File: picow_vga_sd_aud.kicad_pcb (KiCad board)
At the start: 2 copper layers, 74.4 x 53.1 mm, 98 parts, among them J1 10103594-0001LF, J10 Micro_SD_Card, J2 AudioJack3, J3 Micro_SD_Card, J4 L77HDE15SD1CH4F, J5 TSW-102-07-G-S, J6 Conn_01x18_Pin, J7 Conn_02x03_Odd_Even, SW1 SW_Push, SW2 SW_Push, SW3 SW_Push, SW4 SW_Push, SW5 SW_boot, U1 TLV70033_SOT23-5, U10 ER_OLEDM0.91_1x-I2C, U2 PicoW, U3 NC7WZ16P6X, U4 NCP1117ST33T3G, U5 W25Q128JVSIQ, U6 RP2040, U7 W25Q128JVSIQ, U8 TXS0108, U9 TXS0108, X1 12MHz

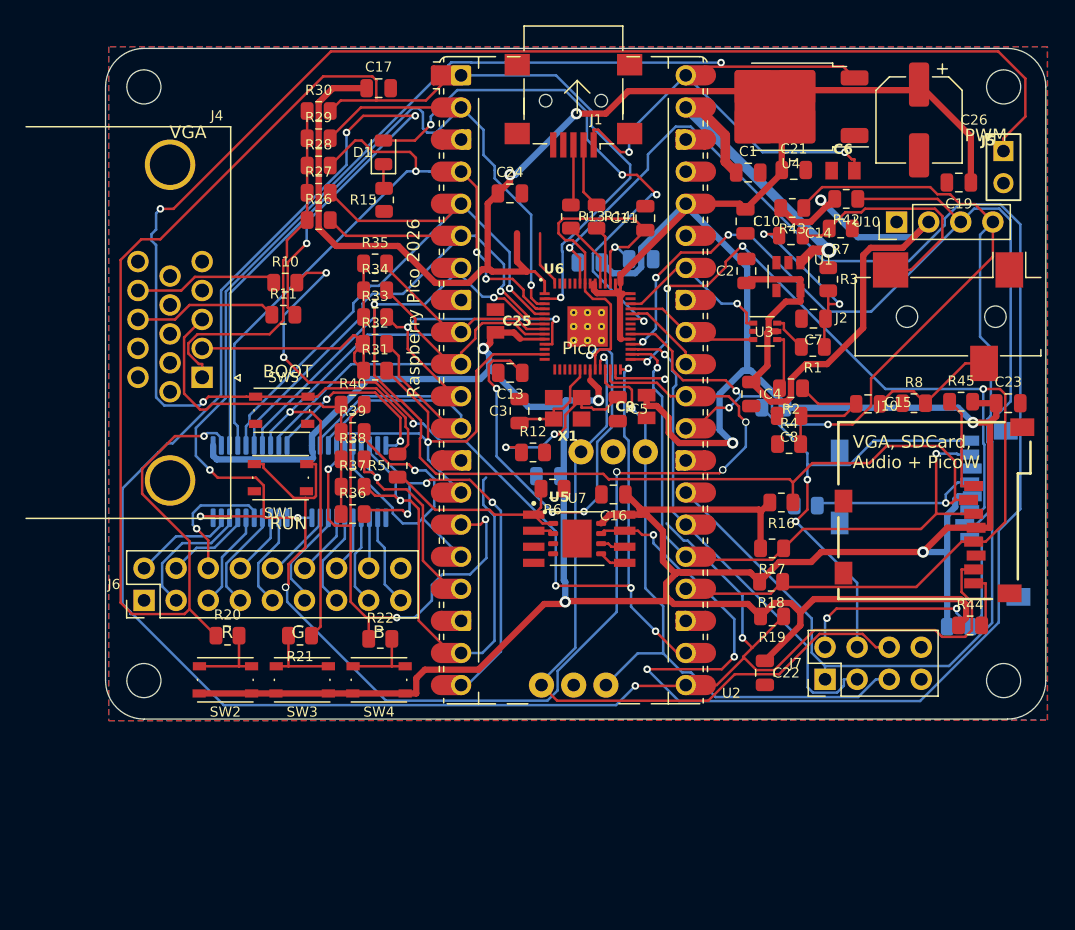
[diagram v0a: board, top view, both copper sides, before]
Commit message: Últimos cambios: referencias Arial, clearances net classes, vias 0.6mm
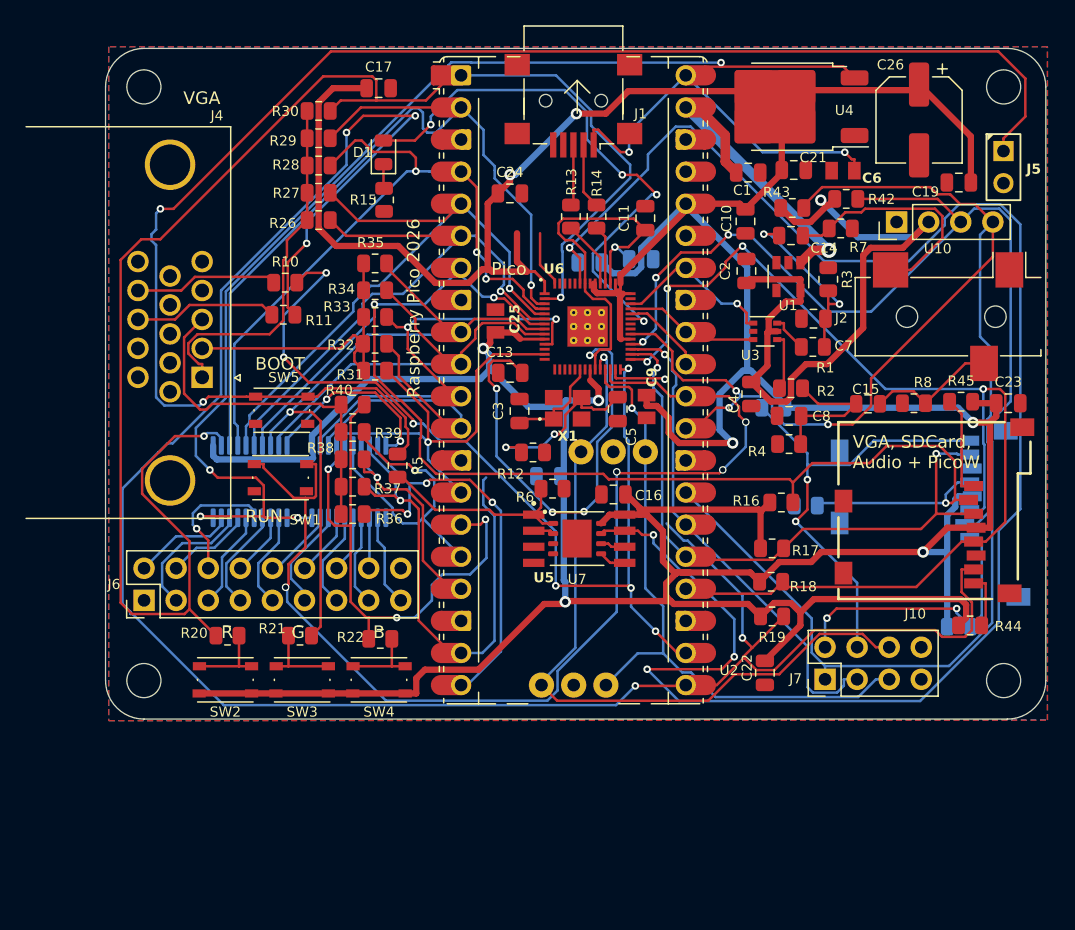
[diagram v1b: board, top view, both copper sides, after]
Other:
- board text removed: "PWM"

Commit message: Cambios adicionales en PCB
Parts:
- added J8: TSW-102-07-G-S, RaspberryPI PicoW:samtec_tsw-102-07-g-s, F.Cu at (157.0, 51.3)
- added L1: 100mH, Resistor_SMD:R_2512_6332Metric, F.Cu at (148.1, 51.0)
- C10, C11, C13, C17, C24, C3, C5: footprint Capacitor_SMD:C_0805_2012Metric -> Capacitor_SMD:C_0603_1608Metric
- C9: footprint RaspberryPI PicoW:generic_capc2012x125 -> Capacitor_SMD:C_0603_1608Metric
- R12: footprint Resistor_SMD:R_0805_2012Metric -> Resistor_SMD:R_0603_1608Metric
- R9: moved to F.Cu
- U5: moved to B.Cu
- moved J5 59.7 mm to (105.2, 51.8), turned to 0 degrees
- moved U7 27.2 mm to (126.9, 60.3)
- moved U5 27.2 mm to (127.2, 60.3), turned to 180 degrees
- moved R43 17.9 mm to (165.7, 61.7), turned to 90 degrees
- moved R24 15.9 mm to (161.5, 81.5), turned to 180 degrees
- moved R42 11.4 mm to (163.4, 61.7), turned to 90 degrees
- moved R12 9.29 mm to (132.3, 72.6), turned to 180 degrees
- moved R5 7.73 mm to (109.0, 80.2), turned to 180 degrees
- moved H3 7.63 mm to (164.8, 106.1)
- moved H4 7.62 mm to (96.5, 106.1)
- moved J7 7.54 mm to (149.3, 105.9)
- moved R23 6.92 mm to (157.2, 100.0)
- moved R20 6.86 mm to (103.1, 101.8)
- moved R21 6.86 mm to (108.9, 101.8)
- moved R22 6.86 mm to (115.2, 102.1)
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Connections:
- C2 pad 1: +3.3VA -> +3V3
- C4 pad 1: +3.3VA -> +3V3
- C6 pad 1: VBUS -> Net-(U4-IN)
- R42 pad 2: +3.3VA -> +3V3
- R43 pad 2: +3.3VA -> +3V3
- U1 pad 5: +3.3VA -> +3V3
- U10 pad 2: +3.3VA -> +3V3
- U3 pad 5: +3.3VA -> +3V3
- U4 pad 3: VBUS -> Net-(U4-IN)
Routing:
- net +3V3: track 411.5 -> 0.00 mm, vias 8 -> 0
- net /GPIO16: track 173.8 -> 0.00 mm, vias 6 -> 0
- net /pico/QSPI_SD3: track 138.7 -> 0.00 mm, vias 4 -> 0
- net /GPIO0: track 127.6 -> 0.00 mm, vias 2 -> 0
- net VBUS: track 123.6 -> 0.00 mm, vias 6 -> 0
- net /pico/~{USB_BOOT}: track 121.2 -> 0.00 mm, vias 2 -> 0
- net /GPIO21: track 118.6 -> 0.00 mm, vias 3 -> 0
- net /GPIO5: track 110.9 -> 0.00 mm, vias 3 -> 0
- net /GPIO22: track 91.1 -> 0.00 mm, vias 3 -> 0
- net /GPIO18: track 90.0 -> 0.00 mm, vias 4 -> 0
- net /RUN: track 89.1 -> 0.00 mm, vias 4 -> 0
- net /GPIO17: track 75.0 -> 0.00 mm, vias 7 -> 0
- net /GPIO1: track 68.9 -> 0.00 mm, vias 1 -> 0
- net +1V1: track 65.4 -> 0.00 mm, vias 5 -> 0
- net /SWCLK: track 59.9 -> 0.00 mm, vias 1 -> 0
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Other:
- board size 74.4 x 53.1 mm -> 74.4 x 60.7 mm

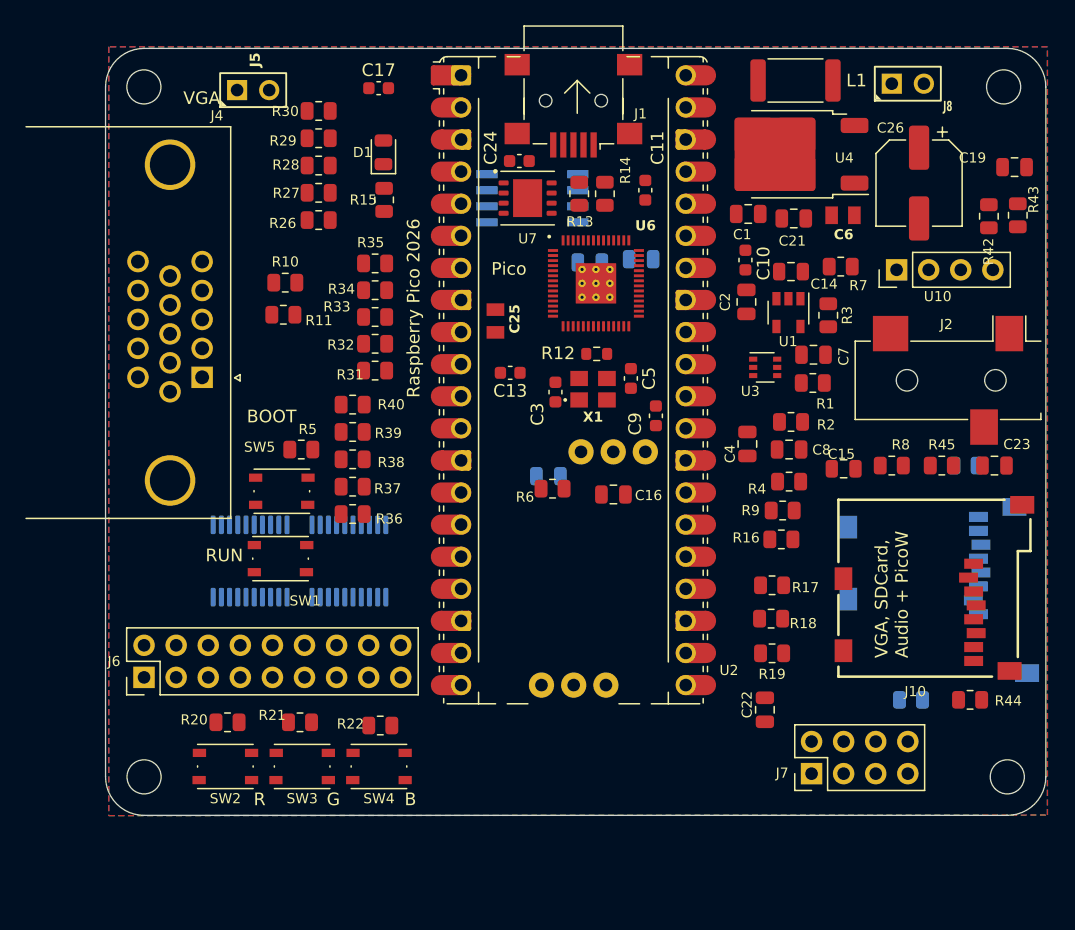
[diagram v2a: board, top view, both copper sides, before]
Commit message: Actualizar archivos del proyecto KiCad
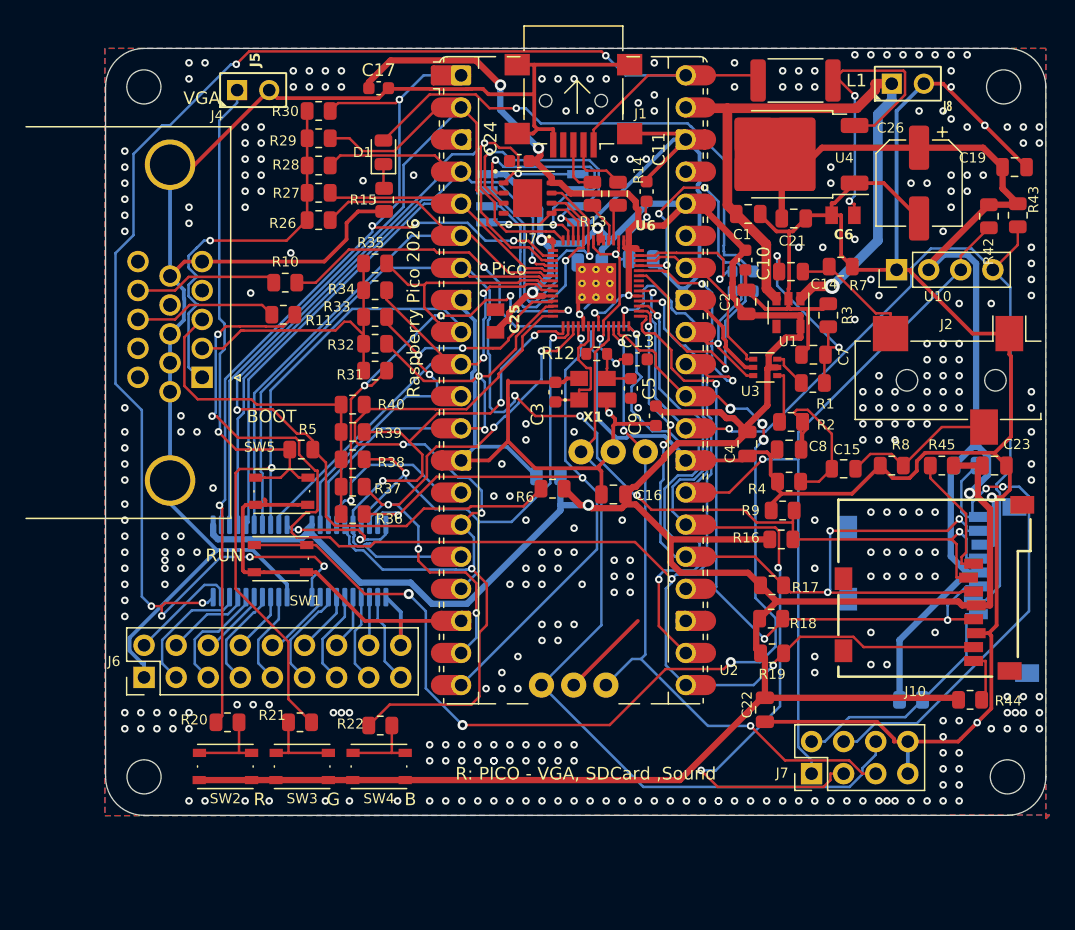
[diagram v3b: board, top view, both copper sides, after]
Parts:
- added R25: 10k, Resistor_SMD:R_0603_1608Metric, B.Cu at (143.9, 66.1)
- added R41: 1K, Resistor_SMD:R_0603_1608Metric, B.Cu at (143.9, 67.7)
- moved C13 10.1 mm to (135.6, 73.1), turned to 0 degrees
- moved R13 1.04 mm to (132.0, 60.0)
- moved R14 1.04 mm to (134.0, 60.0)
- moved C5 0.79 mm to (135.0, 75.4)
- moved C11 0.14 mm to (136.3, 59.8)
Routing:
- net GND: track 0.00 -> 477.7 mm, vias 0 -> 324
- net +3V3: track 0.00 -> 402.4 mm, vias 0 -> 9
- net /GPIO16: track 0.00 -> 129.9 mm, vias 0 -> 5
- net VBUS: track 0.00 -> 125.5 mm, vias 0 -> 7
- net /GPIO5: track 0.00 -> 104.7 mm, vias 0 -> 4
- net /RUN: track 0.00 -> 87.4 mm, vias 0 -> 6
- net /pico/QSPI_SS: track 0.00 -> 85.7 mm, vias 0 -> 3
- net /GPIO0: track 0.00 -> 85.1 mm, vias 0 -> 5
- net /GPIO21: track 0.00 -> 79.3 mm, vias 0 -> 2
- net /GPIO22: track 0.00 -> 78.0 mm, vias 0 -> 2
- net /GPIO11: track 0.00 -> 74.9 mm, vias 0 -> 3
- net /GPIO6: track 0.00 -> 74.5 mm, vias 0 -> 1
- net /GPIO17: track 0.00 -> 71.0 mm, vias 0 -> 3
- net /GPIO1: track 0.00 -> 70.1 mm
- net /GPIO20: track 0.00 -> 64.8 mm, vias 0 -> 3
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- added copper zone on B.Cu, net GND
- added copper zone on F.Cu, net GND
- removed copper zone on B.Cu, net (none)
- removed copper zone on F.Cu, net (none)
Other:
- board text added: "R: PICO - VGA, SDCard ,Sound"
- board text removed: "VGA, SDCard, Audio + PicoW"

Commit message: Últimos cambios del proyecto KiCad
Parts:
- moved SW1 39.1 mm to (146.3, 85.9)
- moved R9 3.76 mm to (147.0, 88.8)
- moved R16 3.54 mm to (146.2, 90.8)
- moved R17 2.57 mm to (146.2, 93.5)
- moved R18 2.16 mm to (146.1, 95.8)
- moved R19 1.73 mm to (146.2, 98.1)
- moved C20 0.84 mm to (131.8, 64.6)
- moved C13 0.66 mm to (136.2, 73.1)
- moved R12 0.43 mm to (132.8, 72.6)
- turned C25 to -90 degrees
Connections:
- J10 pad P$2: (no net) -> GND
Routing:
- net /RUN: track 87.4 -> 26.7 mm, vias 6 -> 2
- net /GPIO27: track 32.8 -> 20.2 mm, vias 4 -> 0
- net /PWM_RR: track 15.8 -> 7.68 mm
- net +3V3: track 402.4 -> 396.1 mm, vias 9 -> 10
- net /GPIO19: track 64.3 -> 70.1 mm, vias 6 -> 7
- net GND: track 477.7 -> 482.0 mm, vias 324 -> 344
- net /GPIO21: track 79.3 -> 82.9 mm
- net /GPIO22: track 78.0 -> 80.3 mm
- net /GPIO16: track 129.9 -> 132.0 mm
- net /pico/QSPI_SD3: track 24.6 -> 26.7 mm
- net VBUS: track 125.5 -> 123.6 mm
- net /GPIO5: track 104.7 -> 106.0 mm
- net /GPIO29: track 11.5 -> 10.3 mm
- net /GPIO20: track 64.8 -> 66.0 mm
- net /GPIO10: track 48.3 -> 47.1 mm
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- added copper zone on In1.Cu, net GND
- added copper zone on In2.Cu, net GND
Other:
- copper layers 2 -> 4

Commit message: Últimos cambios del proyecto KiCad
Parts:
- moved J1 0.13 mm to (130.5, 52.7)
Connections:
- J10 pad P$2: GND -> (no net)
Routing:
- net GND: track 482.0 -> 517.8 mm, vias 344 -> 353
- net /GPIO20: track 66.0 -> 59.0 mm
- net +3V3: track 396.1 -> 400.2 mm
- net /pico/QSPI_SD3: track 26.7 -> 28.4 mm
- net /pico/QSPI_SS: track 85.7 -> 87.4 mm
- net /GPIO5: track 106.0 -> 104.6 mm
- net /GPIO1: track 70.1 -> 71.4 mm
- net /VGA_R: track 30.7 -> 29.6 mm
- net /GPIO19: track 70.1 -> 69.1 mm
- net /GPIO11: track 75.2 -> 74.2 mm
- net /pico/QSPI_SCLK: track 23.3 -> 24.4 mm
- net /logic_convert/B_12: track 9.21 -> 9.96 mm
- net /GPIO13: track 44.1 -> 44.8 mm
- net /GPIO3: track 54.4 -> 55.0 mm
- net /logic_convert/B_14: track 8.05 -> 8.64 mm
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
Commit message: Update schematics and PCB
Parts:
- added C27: 1u, Capacitor_SMD:C_0805_2012Metric, B.Cu at (144.4, 59.4)
- added J9: Mini-DIN-6, kiC:TE_5749180-1, F.Cu at (151.7, 111.5)
- added R46: 1k, Resistor_SMD:R_0805_2012Metric, B.Cu at (143.8, 62.5)
- added R47: 1k, Resistor_SMD:R_0805_2012Metric, B.Cu at (146.1, 57.1)
- added R48: 1k, Resistor_SMD:R_0805_2012Metric, B.Cu at (149.4, 62.5)
- added U11: TL431DBZ, Package_TO_SOT_SMD:SOT-23, B.Cu at (149.4, 58.8)
- C25, C6: footprint RaspberryPI PicoW:generic_capc2012x125 -> Capacitor_SMD:C_0805_2012Metric
- moved J7 22.6 mm to (127.0, 109.1)
- moved SW2 2.82 mm to (102.9, 108.1)
- moved SW3 2.82 mm to (109.0, 108.1)
- moved SW4 2.82 mm to (115.1, 108.1)
- moved J10 0.33 mm to (158.7, 91.2)
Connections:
- U2 pad 35: unconnected-(U2-ADC_VREF-Pad35)_1 -> /GPIO29
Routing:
- net +3V3: track 400.2 -> 453.8 mm, vias 10 -> 14
- net /GPIO27: track 20.2 -> 68.8 mm, vias 0 -> 3
- net /GPIO26: track 18.3 -> 66.3 mm, vias 2 -> 4
- net /VSYS: track 55.0 -> 99.5 mm, vias 1 -> 2
- net /SD_DAT1: track 41.0 -> 85.3 mm
- net /SD_DAT2: track 19.3 -> 56.9 mm
- net /SWCLK: track 64.5 -> 41.9 mm
- net /GPIO21: track 83.1 -> 104.7 mm
- net GND: track 517.8 -> 506.5 mm, vias 353 -> 341
- net /GPIO20: track 59.0 -> 67.5 mm, vias 3 -> 2
- net Net-(C27-Pad1): track 0.00 -> 5.74 mm
- net /SWDIO: track 53.6 -> 58.1 mm
- net /GPIO29: track 10.3 -> 14.5 mm, vias 1 -> 0
- net Net-(R22-Pad2): track 6.29 -> 9.55 mm
- net Net-(U11-REF): track 0.00 -> 3.24 mm
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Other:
- board size 74.4 x 60.7 mm -> 74.4 x 65.8 mm
- board text added: "MICROTECNICA"
- board text added: "R: PICO - VGA, SDCard Sound , Logic convert"
- board text added: "Raspberry Pico"
- board text removed: "R: PICO - VGA, SDCard ,Sound"
- board text removed: "Raspberry Pico 2026"

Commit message: Fix LCSC placements
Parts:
- moved C9 11.3 mm to (129.0, 85.5), turned to 0 degrees
- moved C10 0.61 mm to (143.5, 65.2)
- moved R6 0.33 mm to (128.8, 83.6)
- moved J7 0.08 mm to (127.0, 109.2)
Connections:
- C2 pad 1: +3V3 -> +3.3VA
- C4 pad 1: +3V3 -> +3.3VA
- U1 pad 5: +3V3 -> +3.3VA
- U3 pad 5: +3V3 -> +3.3VA
- U8 pad 10: /logic_convert/OE -> VBUS
- U9 pad 10: /logic_convert/OE -> VBUS
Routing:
- net +3V3: track 453.8 -> 372.2 mm, vias 14 -> 13
- net +3.3VA: track 0.00 -> 14.8 mm
- net VBUS: track 123.2 -> 135.3 mm, vias 7 -> 9
- net /logic_convert/OE: track 9.28 -> 0.00 mm, vias 2 -> 0
- net /GPIO16: track 133.6 -> 128.9 mm
- net /GPIO11: track 74.5 -> 71.9 mm
- net GND: vias 341 -> 338
